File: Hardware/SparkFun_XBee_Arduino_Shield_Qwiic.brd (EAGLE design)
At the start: 53.3 x 59.7 mm, 171 parts, among them J4 QWIIC_RIGHT_ANGLE, Q1 220mA/50V/3.5Ω, Q3 3.1A/30V/105mΩ, Q5 20V/4.2A/52mΩ/1.4W, U1 FSUSB42MUX, U2 AP63203, U3 ESD Diode, U4 FT231XS, U5 ESD Diode, X1 JUMPER-SMT_2_NO_SILK

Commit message: Adds new v11 panel
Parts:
- moved LOGO1 90.4 mm to (0.00, 0.00)
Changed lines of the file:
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@@
 <layers>
 <layer number="1" name="Top" color="4" fill="1" visible="yes" active="yes"/>
-<layer number="2" name="Route2" color="23" fill="1" visible="no" active="yes"/>
-<layer number="15" name="Route15" color="39" fill="1" visible="no" active="yes"/>
+<layer number="2" name="Route2" color="23" fill="1" visible="yes" active="yes"/>
+<layer number="15" name="Route15" color="39" fill="1" visible="yes" active="yes"/>
 <layer number="16" name="Bottom" color="3" fill="1" visible="yes" active="yes"/>
 <layer number="17" name="Pads" color="26" fill="1" visible="yes" active="yes"/>
@@
 <element name="U$86" library="topmirror" package="BOARD1347" value="" x="38.1" y="55.88" smashed="yes"/>
 <element name="U$73" library="top" package="#I2C#13751" value="" x="13.4058" y="17.7892" smashed="yes"/>
-<element name="LOGO1" library="SparkFun-Aesthetics" package="BLANK" value="SFE_LOGO_NAMEBLANK" x="85.09" y="30.48" smashed="yes"/>
+<element name="LOGO1" library="SparkFun-Aesthetics" package="BLANK" value="SFE_LOGO_NAMEBLANK" x="0" y="0" smashed="yes"/>
 <element name="LOGO4" library="SparkFun-Aesthetics" package="ORDERING_INSTRUCTIONS" value="SPECIAL_INSTRUCTIONS-ORDERING" x="77.05" y="56.5" smashed="yes"/>
 <element name="Q5" library="SparkFun-DiscreteSemi" package="SOT23-3" value="20V/4.2A/52mΩ/1.4W" x="30.099" y="27.6606" smashed="yes" rot="R180">

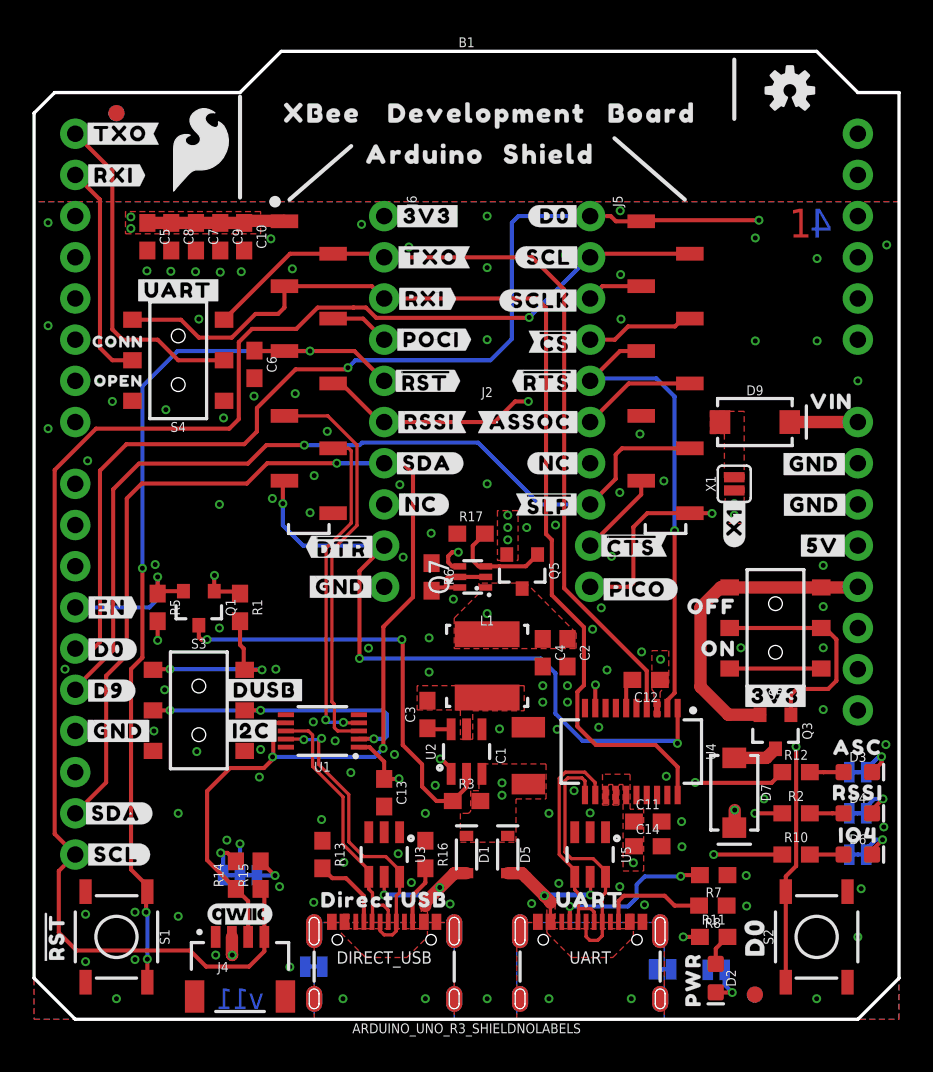
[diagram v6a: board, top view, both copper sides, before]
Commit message: Removes UART and direction communication
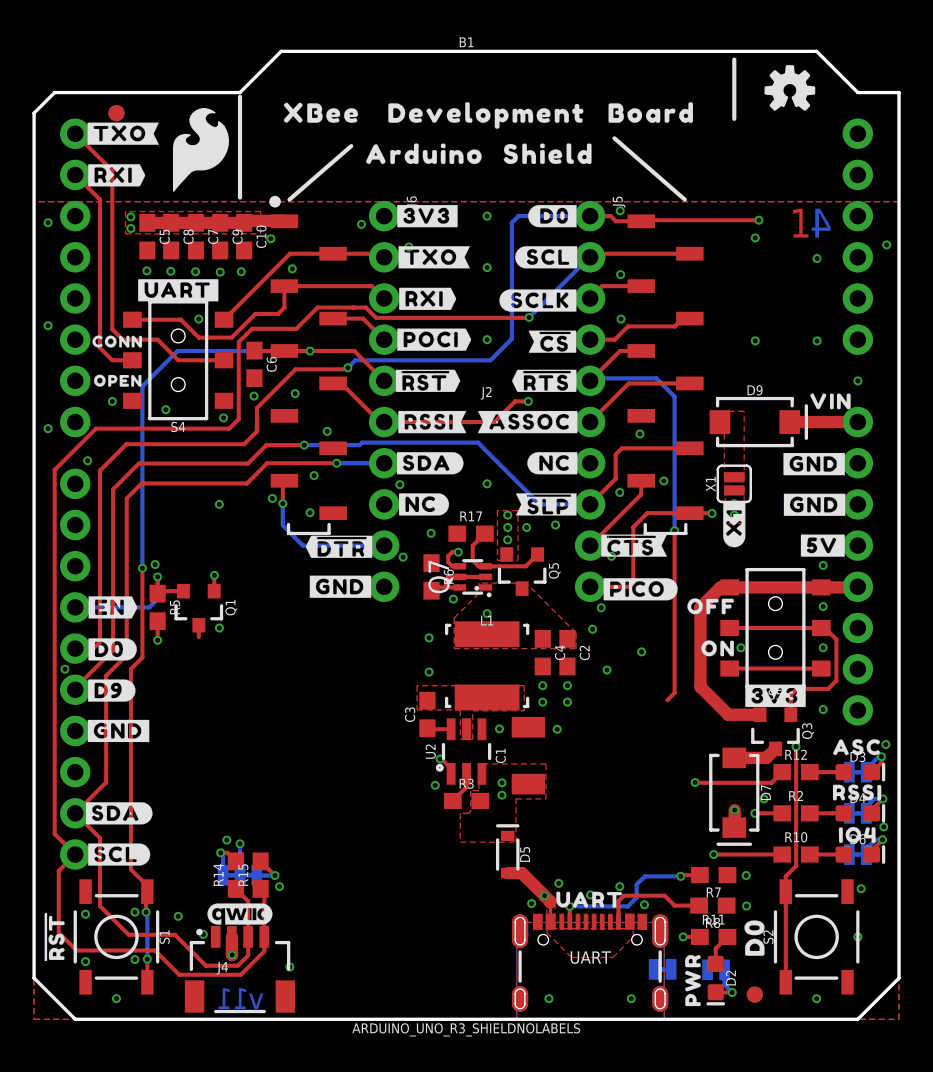
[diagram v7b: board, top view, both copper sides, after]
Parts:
- removed C11, C12, C13: 0.1uF, SparkFun-Capacitors:0603
- removed C14: 4.7uF, SparkFun-Capacitors:0603
- removed D1: 3A/10V/280mV, SparkFun-DiscreteSemi:SOD-323
- removed DIRECT_USB: USB Female Type C Connector, SparkFun-Connectors:USB-C-16P-4LAYER-ISOLATED
- removed R1: 100k, SparkFun-Resistors:0603
- removed R13, R16: 5.1k, SparkFun-Resistors:0603
- removed S3: (no value), SparkFun-Switches:SWITCH_DPDT_SMD_AYZ0202
- removed SHLD1: JUMPER-SMT_2_NC_TRACE_SILK, SparkFun-Jumpers:SMT-JUMPER_2_NC_TRACE_SILK
- removed U$71: (no value), topmirror:DIRECT_USB33
- removed U$72: (no value), botmirror:#DUSB#31
- removed U$73: (no value), top:#I2C#13751
- removed U$75: (no value), topmirror:#SHLD1#37
- removed U1: FSUSB42MUX, SparkFun-IC-Special-Function:MSOP10
- removed U3, U5: ESD Diode, SparkFun-DiscreteSemi:SOT-23-6
- removed U4: FT231XS, SparkFun-IC-Comms:SSOP20_L
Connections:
- removed net D+: U4.11, U5.6, UART.A6, UART.B6
- removed net D-: U4.12, U5.4, UART.A7, UART.B7
- removed net DIRECT_D+: DIRECT_USB.A6, DIRECT_USB.B6, U1.9, U3.6
- removed net DIRECT_D-: DIRECT_USB.A7, DIRECT_USB.B7, U1.8, U3.4
- removed net DIRECT_SELECT: S3.2, S3.5, U1.2
- removed net DIRECT_USB: R1.2, S3.1, S3.4
- removed net N$14: DIRECT_USB.B5, R16.2
- removed net N$15: DIRECT_USB.A5, R13.2
- removed net SHLD1: DIRECT_USB.SHLD1, DIRECT_USB.SHLD2, DIRECT_USB.SHLD3, DIRECT_USB.SHLD4, DIRECT_USB.SHLD5, DIRECT_USB.SHLD6, DIRECT_USB.SHLD7, DIRECT_USB.SHLD8, SHLD1.2
- removed net V_USB_2: D1.A, DIRECT_USB.VBUS1, DIRECT_USB.VBUS2, U3.5
- net 3.3V: no longer C11.1, C12.1, C13.1, C14.1, R1.1, U1.1, U4.13, U4.14, U4.15, U4.3
- net D11/SDA: no longer U1.7
- net D13/TXO: no longer U4.4
- net D14/RXI: no longer U4.20
- net D6/!RTS!: no longer U4.2
- net D7/!CTS!: no longer U4.9
- net D8/!DTR!: no longer U4.1
- net GND: no longer C11.2, C12.2, C13.2, C14.2, DIRECT_USB.GND, DIRECT_USB.GND2, R13.1, R16.1, S3.3, S3.6, SHLD1.1, U1.10, U1.5, U3.2, U4.16, U4.6, U5.2
- net VCC: no longer D1.C
- net V_USB: no longer U5.5
- net XBEE_D+/SDA: no longer U1.3
- net XBEE_D-: no longer U1.4
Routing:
- net D14/RXI: track 64.5 -> 18.4 mm
- net D13/TXO: track 51.5 -> 11.7 mm
- net D8/!DTR!: track 42.6 -> 9.56 mm, vias 3 -> 1
- net XBEE_D+/SDA: track 24.9 -> 0.00 mm
- net EN: track 27.2 -> 2.75 mm, vias 2 -> 0
- net D11/SDA: track 82.2 -> 59.2 mm, vias 3 -> 1
- net XBEE_D-: track 20.5 -> 0.00 mm, vias 2 -> 0
- net DIRECT_D+: track 18.9 -> 0.00 mm, vias 2 -> 0
- net DIRECT_SELECT: track 18.7 -> 0.00 mm, vias 3 -> 0
- net DIRECT_D-: track 16.6 -> 0.00 mm
- net D+: track 15.8 -> 0.00 mm
- net D-: track 14.4 -> 0.00 mm
- net D7/!CTS!: track 18.1 -> 6.24 mm, vias 1 -> 0
- net DIRECT_USB: track 11.0 -> 0.00 mm, vias 2 -> 0
- net V_USB_2: track 9.83 -> 0.00 mm, vias 2 -> 0
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- removed copper zone on layer 1, net SHLD1
- removed copper zone on layer 16, net SHLD1
- removed copper zone on layer 1, net V_USB_2

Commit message: Moves USB-C to center of board
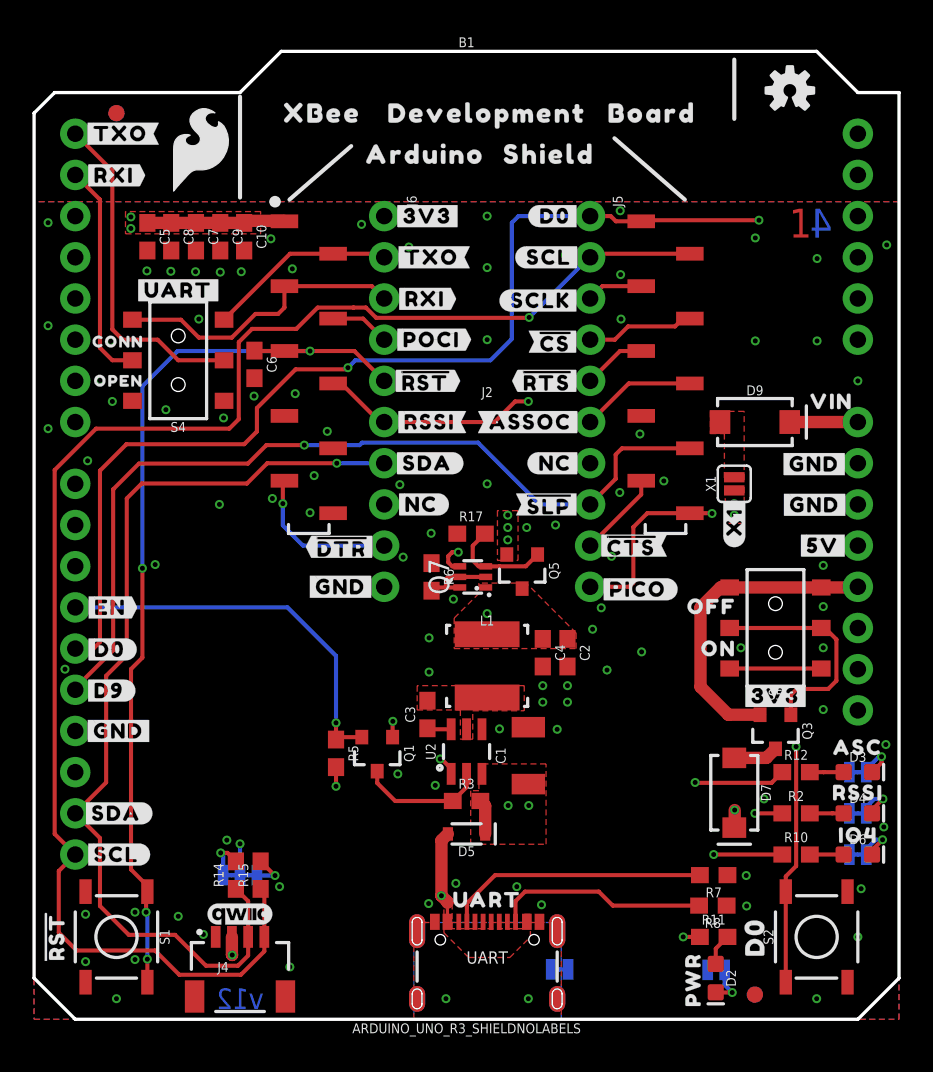
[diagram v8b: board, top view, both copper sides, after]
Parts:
- moved Q1 14.2 mm to (21.2, 16.4)
- moved R5 14.2 mm to (18.6, 16.4)
- moved U$28 6.35 mm to (27.9, 7.37)
- moved U$4 6.35 mm to (29.0, 3.05)
- moved UART 6.35 mm to (27.9, 6.35)
- moved SHLD 6.35 mm to (32.4, 3.07)
- moved D5 2.84 mm to (26.7, 11.4), turned to 180 degrees
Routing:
- net D6/!RTS!: track 28.6 -> 3.91 mm, vias 1 -> 0
- net EN-TRANS: track 9.34 -> 24.1 mm
- net N$5: track 6.64 -> 13.2 mm
- net N$6: track 10.3 -> 16.2 mm, vias 2 -> 0
- net EN: track 2.75 -> 7.87 mm
- net VCC: track 28.1 -> 32.7 mm
- net V_USB: track 4.61 -> 5.75 mm, vias 2 -> 1
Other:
- board text added: "v12"
- board text removed: "v11"
